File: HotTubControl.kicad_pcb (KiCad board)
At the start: 2 copper layers, 90 x 90 mm, 33 parts, among them J1 Wasser Vorlauf, J2 Wasser Rücklauf, J3 Massagepumpe, J4 Filterpumpe, J5 Füllstandsensor, J6 Wagoklemme-4polig236-504_332-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, K1 JV-KT, K2 JV-KT, Q1 BC337, Q2 BSS138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

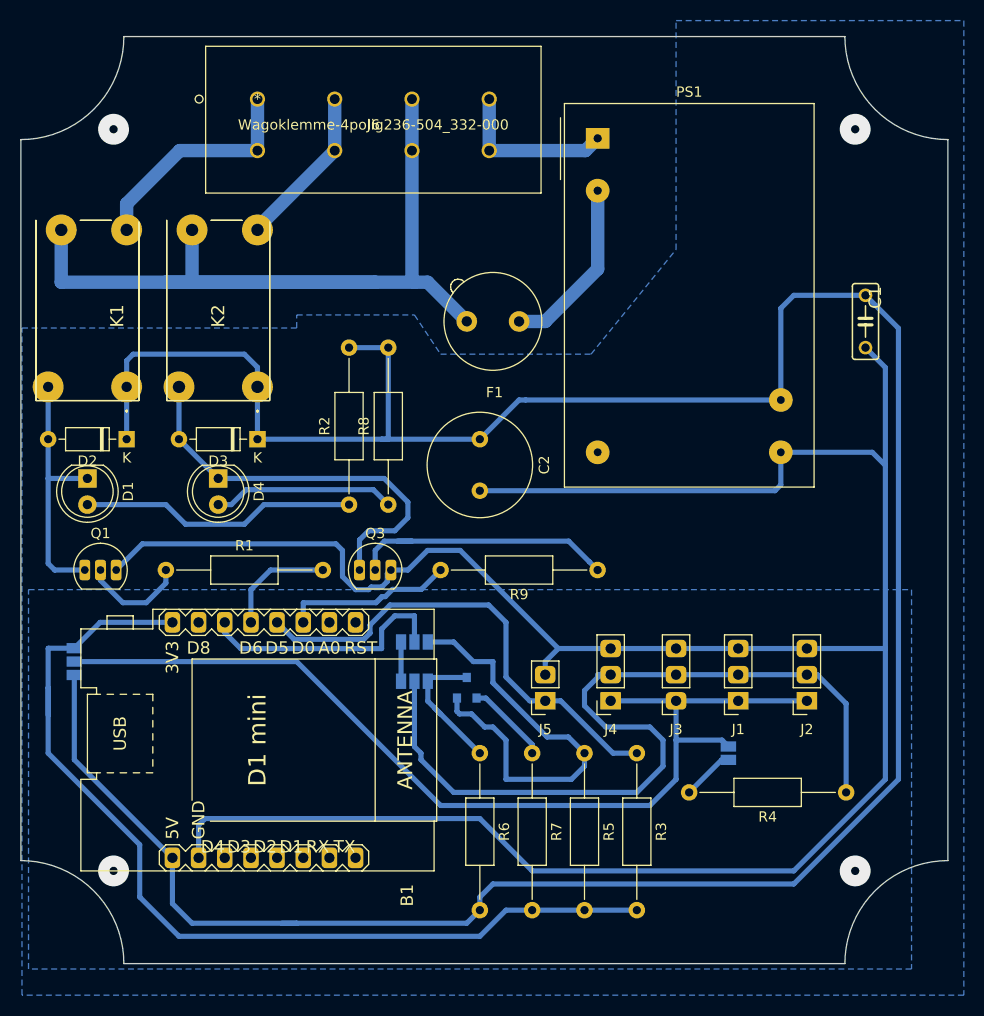
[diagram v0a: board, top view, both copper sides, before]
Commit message: Anpassung Ausfüllungen
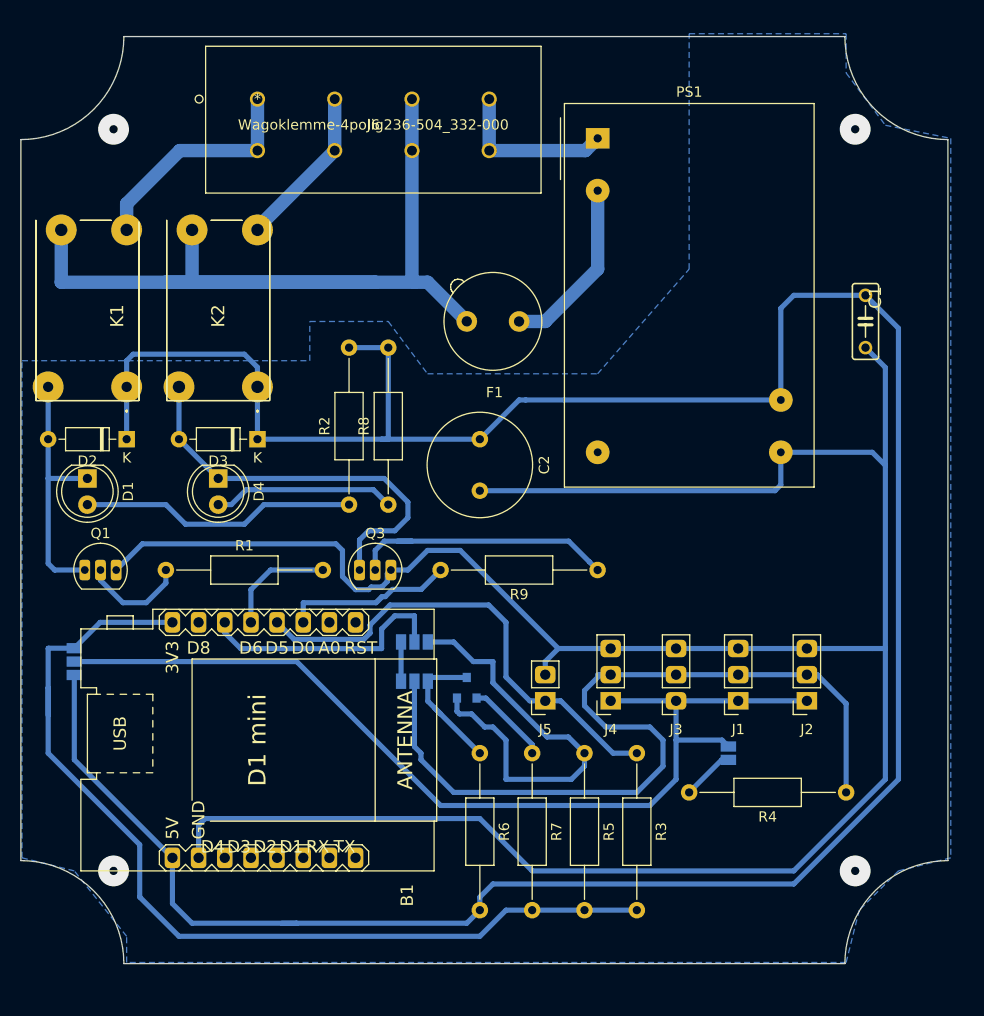
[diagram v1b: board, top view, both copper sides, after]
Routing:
- removed copper zone on B.Cu, net GND

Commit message: with ibom
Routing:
- net Net-(J6-Pad3): track 15.8 -> 18.0 mm
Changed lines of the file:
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@@
     (thickness 1.6)
     (drawings 8)
-    (tracks 246)
+    (tracks 247)
     (zones 0)
     (modules 33)
@@
     (add_net "Net-(Q2-Pad1)")
     (add_net "Net-(Q3-Pad2)")
+  )
+  (module ene9ba_footprint:WAGOKlemme4pol (layer F.Cu)
+    (at 79.25 63.42)
+    (fp_text reference J6 (at 11.25 2.5) (layer F.SilkS)
+      (effects (font (size 1 1) (thickness 0.15)))
+    )
+    (fp_text value Wagoklemme-4polig236-504_332-000 (at 11.25 2.5) (layer F.SilkS)
+      (effects (font (size 1 1) (thickness 0.15)))
+    )
+    (fp_line (start -5.0314 9.122415) (end 27.5314 9.122415) (layer F.SilkS) (width 0.12))
+    (fp_line (start 27.5314 9.122415) (end 27.5314 -5.126985) (layer F.SilkS) (width 0.12))
+    (fp_line (start 27.5314 -5.126985) (end -5.0314 -5.126985) (layer F.SilkS) (width 0.12))
+    (fp_line (start -5.0314 -5.126985) (end -5.0314 9.122415) (layer F.SilkS) (width 0.12))
+    (fp_line (start -4.9044 8.995415) (end 27.4044 8.995415) (layer F.Fab) (width 0.1))
+    (fp_line (start 27.4044 8.995415) (end 27.4044 -4.999985) (layer F.Fab) (width 0.1))
+    (fp_line (start 27.4044 -4.999985) (end -4.9044 -4.999985) (layer F.Fab) (width 0.1))
+    (fp_line (start -4.9044 -4.999985) (end -4.9044 8.995415) (layer F.Fab) (width 0.1))
+    (fp_line (start -5.1584 -5.253985) (end -5.1584 9.249415) (layer F.CrtYd) (width 0.05))
+    (fp_line (start -5.1584 9.249415) (end 27.6584 9.249415) (layer F.CrtYd) (width 0.05))
+    (fp_line (start 27.6584 9.249415) (end 27.6584 -5.253985) (layer F.CrtYd) (width 0.05))
+    (fp_line (start 27.6584 -5.253985) (end -5.1584 -5.253985) (layer F.CrtYd) (width 0.05))
+    (fp_circle (center 0 -1.905) (end 0.381 -1.905) (layer F.Fab) (width 0.1))
+    (fp_circle (center -5.6664 0) (end -5.2854 0) (layer F.SilkS) (width 0.12))
+    (fp_circle (center -5.6664 0) (end -5.2854 0) (layer B.SilkS) (width 0.12))
+    (fp_text user * (at 0 0) (layer F.Fab)
+      (effects (font (size 1 1) (thickness 0.15)))
+    )
+    (fp_text user * (at 0 0) (layer F.SilkS)
+      (effects (font (size 1 1) (thickness 0.15)))
+    )
+    (fp_text user "Copyright 2021 Accelerated Designs. All rights reserved." (at 0 0) (layer Cmts.User)
+      (effects (font (size 0.127 0.127) (thickness 0.002)))
+    )
+    (pad 8 thru_hole rect (at 22.5 5) (size 3.5 3.5) (drill 1) (layers *.Cu *.Mask)
+      (net 23 "Net-(J6-Pad7)"))
+    (pad 7 thru_hole rect (at 22.5 0) (size 3.5 3.5) (drill 1) (layers *.Cu *.Mask)
+      (net 23 "Net-(J6-Pad7)"))
+    (pad 6 thru_hole rect (at 15 5) (size 3.5 3.5) (drill 1) (layers *.Cu *.Mask)
+      (net 7 "Net-(F1-Pad2)"))
+    (pad 5 thru_hole rect (at 15 0) (size 3.5 3.5) (drill 1) (layers *.Cu *.Mask)
+      (net 7 "Net-(F1-Pad2)"))
+    (pad 4 thru_hole rect (at 7.5 5) (size 3.5 3.5) (drill 1) (layers *.Cu *.Mask)
+      (net 24 "Net-(J6-Pad3)"))
+    (pad 3 thru_hole rect (at 7.5 0) (size 3.5 3.5) (drill 1) (layers *.Cu *.Mask)
+      (net 24 "Net-(J6-Pad3)"))
+    (pad 2 thru_hole rect (at 0 5) (size 3.5 3.5) (drill 1) (layers *.Cu *.Mask)
+      (net 25 "Net-(J6-Pad1)"))
+    (pad 1 thru_hole rect (at 0 0) (size 3.5 3.5) (drill 1) (layers *.Cu *.Mask)
+      (net 25 "Net-(J6-Pad1)"))
+    (model ${KIPRJMOD}/3D-step/236-504_332-000.stp
+      (offset (xyz 28 0 0))
+      (scale (xyz 1 1 1))
+      (rotate (xyz -90 0 90))
+    )
   )
   (module Package_TO_SOT_THT:TO-92_Inline (layer F.Cu)
@@
     (model ${KIPRJMOD}/3D-step/IRM-03-5.stp
       (offset (xyz 8.5 -15 0))
-      (scale (xyz 1 1 1))
-      (rotate (xyz -90 0 90))
-    )
-  )
-  (module ene9ba_footprint:WAGOKlemme4pol (layer F.Cu)
-    (at 79.25 63.42)
-    (fp_text reference J6 (at 11.25 2.5) (layer F.SilkS)
-      (effects (font (size 1 1) (thickness 0.15)))
-    )
-    (fp_text value Wagoklemme-4polig236-504_332-000 (at 11.25 2.5) (layer F.SilkS)
-      (effects (font (size 1 1) (thickness 0.15)))
-    )
-    (fp_line (start -5.0314 9.122415) (end 27.5314 9.122415) (layer F.SilkS) (width 0.12))
-    (fp_line (start 27.5314 9.122415) (end 27.5314 -5.126985) (layer F.SilkS) (width 0.12))
-    (fp_line (start 27.5314 -5.126985) (end -5.0314 -5.126985) (layer F.SilkS) (width 0.12))
-    (fp_line (start -5.0314 -5.126985) (end -5.0314 9.122415) (layer F.SilkS) (width 0.12))
-    (fp_line (start -4.9044 8.995415) (end 27.4044 8.995415) (layer F.Fab) (width 0.1))
-    (fp_line (start 27.4044 8.995415) (end 27.4044 -4.999985) (layer F.Fab) (width 0.1))
-    (fp_line (start 27.4044 -4.999985) (end -4.9044 -4.999985) (layer F.Fab) (width 0.1))
-    (fp_line (start -4.9044 -4.999985) (end -4.9044 8.995415) (layer F.Fab) (width 0.1))
-    (fp_line (start -5.1584 -5.253985) (end -5.1584 9.249415) (layer F.CrtYd) (width 0.05))
-    (fp_line (start -5.1584 9.249415) (end 27.6584 9.249415) (layer F.CrtYd) (width 0.05))
-    (fp_line (start 27.6584 9.249415) (end 27.6584 -5.253985) (layer F.CrtYd) (width 0.05))
-    (fp_line (start 27.6584 -5.253985) (end -5.1584 -5.253985) (layer F.CrtYd) (width 0.05))
-    (fp_circle (center 0 -1.905) (end 0.381 -1.905) (layer F.Fab) (width 0.1))
-    (fp_circle (center -5.6664 0) (end -5.2854 0) (layer F.SilkS) (width 0.12))
-    (fp_circle (center -5.6664 0) (end -5.2854 0) (layer B.SilkS) (width 0.12))
-    (fp_text user * (at 0 0) (layer F.Fab)
-      (effects (font (size 1 1) (thickness 0.15)))
-    )
-    (fp_text user * (at 0 0) (layer F.SilkS)
-      (effects (font (size 1 1) (thickness 0.15)))
-    )
-    (fp_text user "Copyright 2021 Accelerated Designs. All rights reserved." (at 0 0) (layer Cmts.User)
-      (effects (font (size 0.127 0.127) (thickness 0.002)))
-    )
-    (pad 8 thru_hole circle (at 22.5 5) (size 1.4732 1.4732) (drill 0.9652) (layers *.Cu *.Mask)
-      (net 23 "Net-(J6-Pad7)"))
-    (pad 7 thru_hole circle (at 22.5 0) (size 1.4732 1.4732) (drill 0.9652) (layers *.Cu *.Mask)
-      (net 23 "Net-(J6-Pad7)"))
-    (pad 6 thru_hole circle (at 15 5) (size 1.4732 1.4732) (drill 0.9652) (layers *.Cu *.Mask)
-      (net 7 "Net-(F1-Pad2)"))
-    (pad 5 thru_hole circle (at 15 0) (size 1.4732 1.4732) (drill 0.9652) (layers *.Cu *.Mask)
-      (net 7 "Net-(F1-Pad2)"))
-    (pad 4 thru_hole circle (at 7.5 5) (size 1.4732 1.4732) (drill 0.9652) (layers *.Cu *.Mask)
-      (net 24 "Net-(J6-Pad3)"))
-    (pad 3 thru_hole circle (at 7.5 0) (size 1.4732 1.4732) (drill 0.9652) (layers *.Cu *.Mask)
-      (net 24 "Net-(J6-Pad3)"))
-    (pad 2 thru_hole circle (at 0 5) (size 1.4732 1.4732) (drill 0.9652) (layers *.Cu *.Mask)
-      (net 25 "Net-(J6-Pad1)"))
-    (pad 1 thru_hole circle (at 0 0) (size 1.4732 1.4732) (drill 0.9652) (layers *.Cu *.Mask)
-      (net 25 "Net-(J6-Pad1)"))
-    (model ${KIPRJMOD}/3D-step/236-504_332-000.stp
-      (offset (xyz 28 0 0))
       (scale (xyz 1 1 1))
       (rotate (xyz -90 0 90))
@@
   (segment (start 101.75 68.42) (end 111.09 68.42) (width 1.3) (layer B.Cu) (net 23))
   (segment (start 86.75 63.42) (end 86.75 68.42) (width 1.3) (layer B.Cu) (net 24))
-  (segment (start 79.25 75.92) (end 86.75 68.42) (width 1.3) (layer B.Cu) (net 24))
-  (segment (start 79.25 76.12) (end 79.25 75.92) (width 1.3) (layer B.Cu) (net 24))
+  (segment (start 86.75 72.43) (end 86.75 68.42) (width 1.3) (layer B.Cu) (net 24))
+  (segment (start 83.06 76.12) (end 86.75 72.43) (width 1.3) (layer B.Cu) (net 24))
+  (segment (start 79.25 76.12) (end 83.06 76.12) (width 1.3) (layer B.Cu) (net 24))
   (segment (start 79.25 68.42) (end 79.25 63.42) (width 1.3) (layer B.Cu) (net 25))
   (segment (start 71.71 68.42) (end 79.25 68.42) (width 1.3) (layer B.Cu) (net 25))
